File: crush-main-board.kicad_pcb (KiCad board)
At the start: 2 copper layers, 101.6 x 120.6 mm, 46 parts, among them J1 4x4_Header, J10 3x3 Header, J11 3x3 Header, J12 3x2 Header, J13 3x4_Header, J14 3x4_Header, J15 2157601008, J16 Conn_01x02, J17 Conn_01x02, J2 4x4_Header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

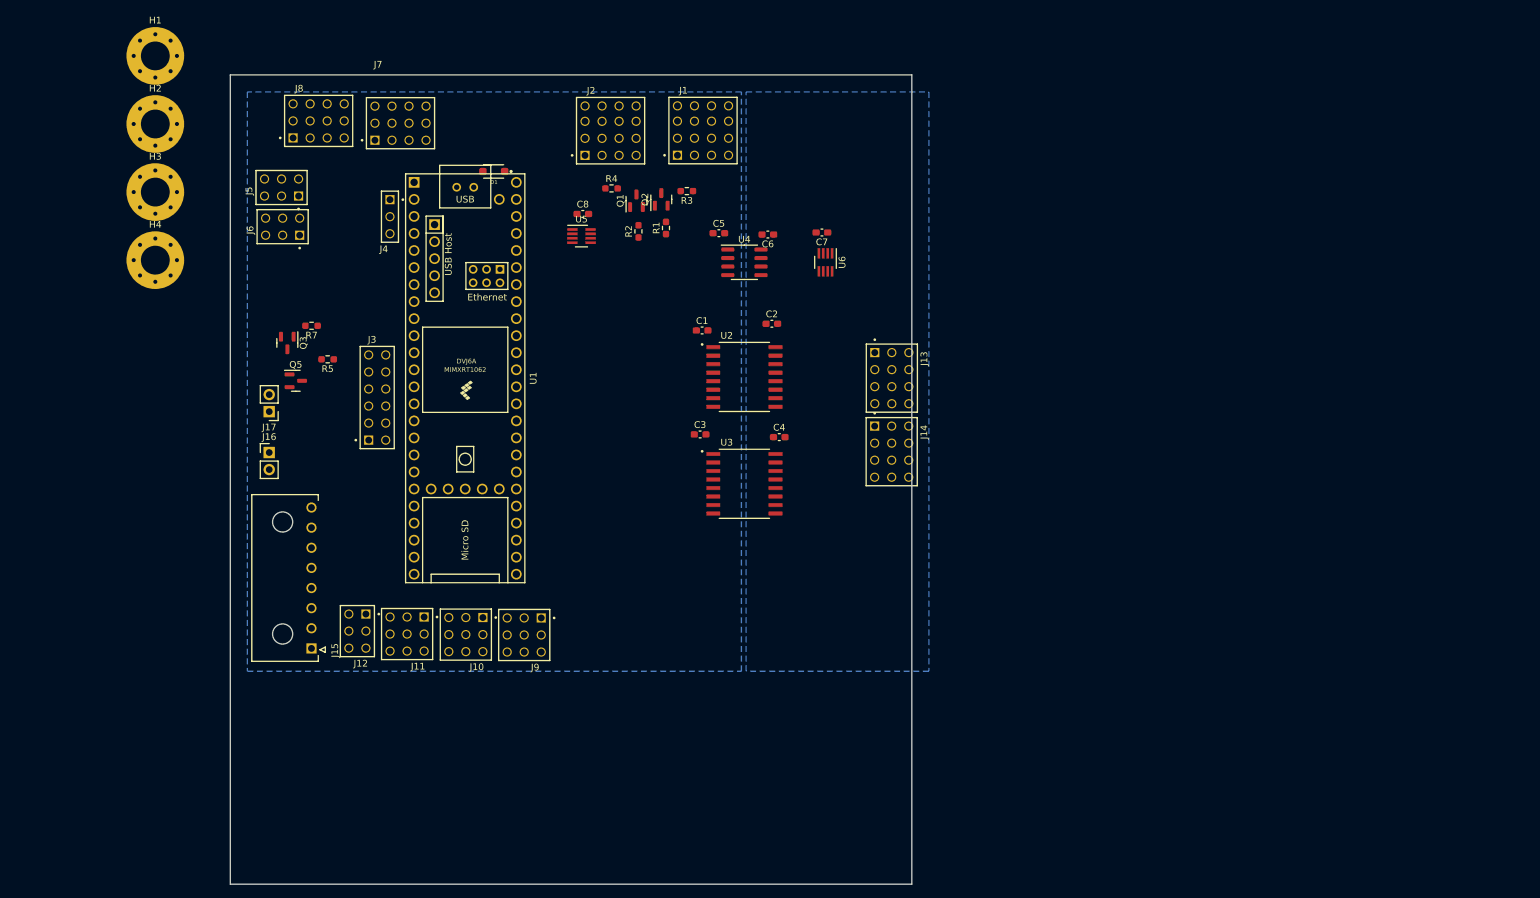
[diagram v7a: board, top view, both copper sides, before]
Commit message: place mounting holes
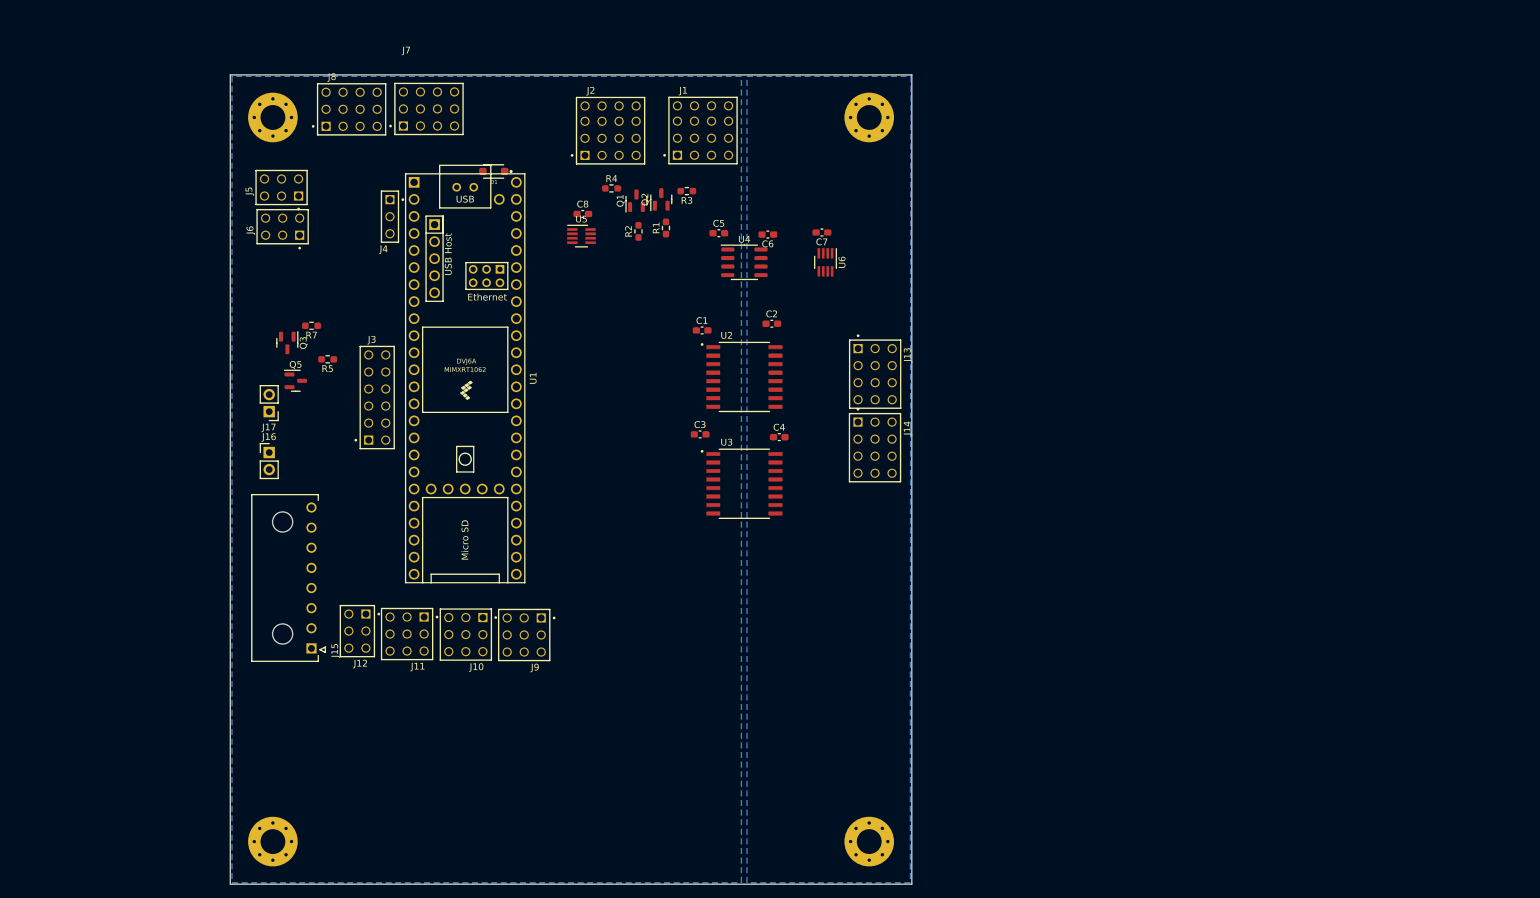
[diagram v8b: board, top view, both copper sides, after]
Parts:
- H1, H2, H3, H4: footprint MountingHole:MountingHole_4.3mm_M4_Pad_Via -> MountingHole:MountingHole_3.7mm_Pad_Via
- moved H3 143.9 mm to (108.0, 127.0)
- moved H2 106.4 mm to (108.0, 19.1)
- moved H4 88.4 mm to (19.1, 127.0)
- moved H1 19.8 mm to (19.1, 19.1)
- moved J8 5.21 mm to (30.8, 17.8)
- moved J7 4.75 mm to (42.3, 17.8)
- moved J14 2.56 mm to (108.8, 68.3)
- moved J13 2.56 mm to (108.8, 57.3)
